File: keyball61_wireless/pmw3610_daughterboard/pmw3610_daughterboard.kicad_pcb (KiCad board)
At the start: 2 copper layers, 24 x 32 mm, 14 parts, among them J1 Conn_Keyball_8pin, U1 PMW3610DM-SUDU, U2 TLV74318PDBVR

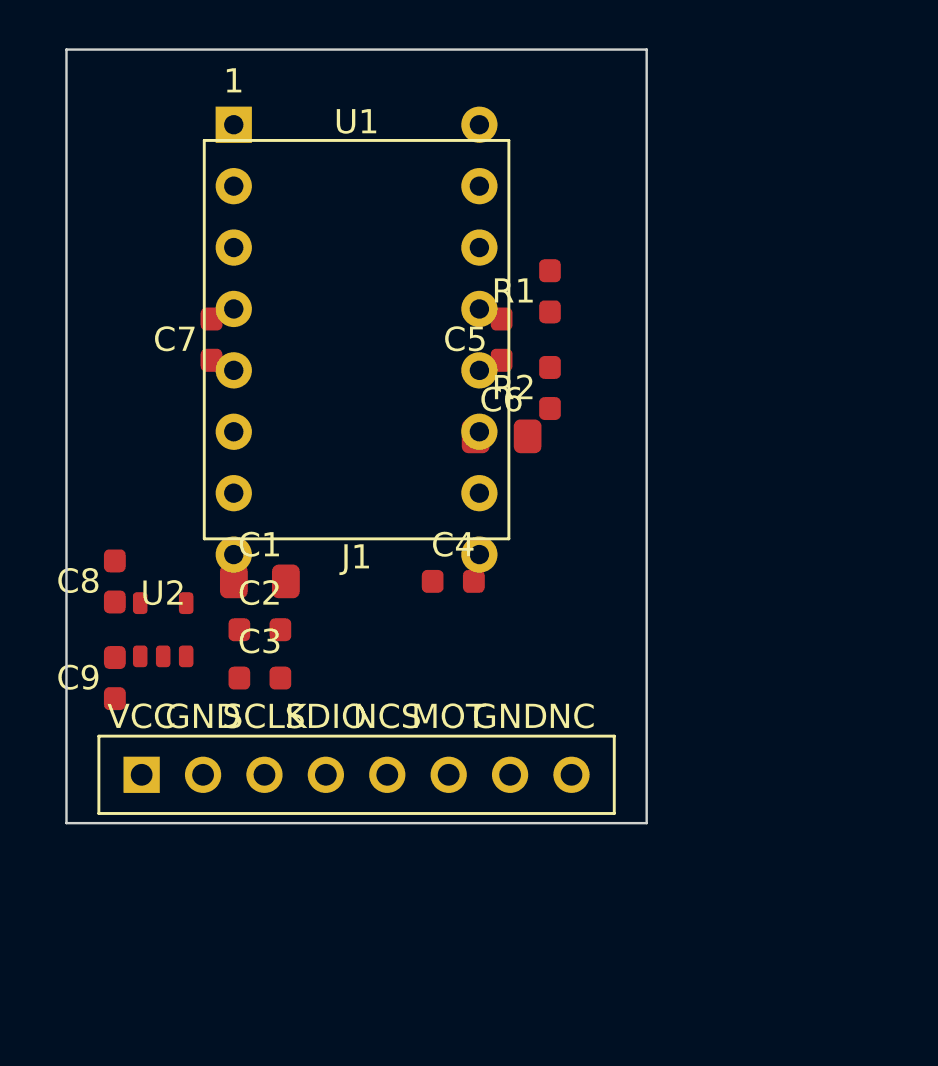
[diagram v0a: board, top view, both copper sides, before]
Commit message: Route PMW3610 daughterboard to DRC-clean fab-ready gerbers
Rebuilt the board with KiCad's native pcbnew API (replacing the kiutils
writer, which emitted KiCad-6 track syntax KiCad 10 rejected), auto-routed
with Freerouting 2.4.1 headless, imported the session, and exported gerbers.

Result: 0 DRC violations, 0 unconnected items. 14 components, 2-layer,
34x40mm, GND pour on B.Cu. Fab package zipped for PCBway.

Pipeline (reproducible):
- build_board.py  : place + net + design rules (pcbnew)
- export_dsn.py   : ExportSpecctraDSN
- Freerouting     : headless auto-route (.dsn -> .ses)
- import_ses.py   : ImportSpecctraSES + zone fill
- fix_track_width.py : widen any sub-0.25mm trace
- make_fab.sh     : end-to-end orchestration
- kicad-cli       : DRC + gerber/drill export

Outputs: gerbers/ (7 gerber + 4 drill), pmw3610_daughterboard_gerbers.zip,
board_top.png render.
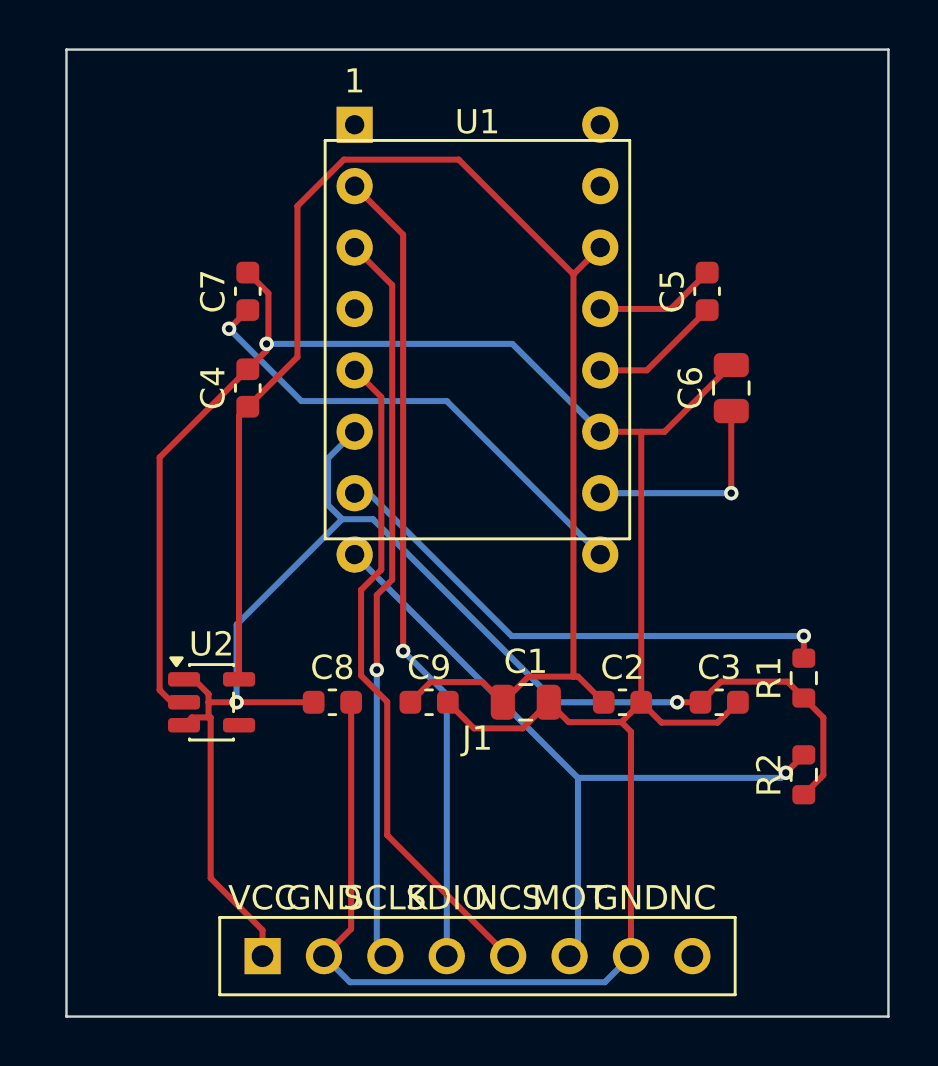
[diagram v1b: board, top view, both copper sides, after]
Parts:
- C1, C6: footprint Capacitor_SMD:C_0805_2012Metric -> C_0805_2012Metric
- C2, C3, C4, C5, C7, C8, C9: footprint Capacitor_SMD:C_0603_1608Metric -> C_0603_1608Metric
- J1: footprint pmw3610_kb:Conn_Keyball_8pin -> Conn_Keyball_8pin
- R1, R2: footprint Resistor_SMD:R_0603_1608Metric -> R_0603_1608Metric
- U1: footprint pmw3610_kb:PMW3610DM-SUDU -> PMW3610DM-SUDU
- U2: footprint Package_TO_SOT_SMD:SOT-23-5 -> SOT-23-5
- moved R1 19.1 mm to (30.5, 26.0)
- moved R2 19.1 mm to (30.5, 30.0)
- moved C3 19.0 mm to (27.0, 27.0)
- moved C2 15.3 mm to (23.0, 27.0)
- moved C9 13.0 mm to (15.0, 27.0), turned to 0 degrees
- moved C1 12.1 mm to (19.0, 27.0)
- moved C4 11.7 mm to (7.50, 14.0), turned to 90 degrees
- moved C8 10.3 mm to (11.0, 27.0), turned to 0 degrees
- moved C6 9.71 mm to (27.5, 14.0), turned to 90 degrees
- moved J1 9.01 mm to (17.0, 37.5)
- moved C5 8.73 mm to (26.5, 10.0)
- moved U1 5.00 mm to (17.0, 12.0)
- moved U2 3.61 mm to (6.00, 27.0)
- moved C7 2.50 mm to (7.50, 10.0)
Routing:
- net GND: track 0.00 -> 102.4 mm, vias 0 -> 1
- net +1V8: track 0.00 -> 62.5 mm
- net +3V3: track 0.00 -> 59.8 mm, vias 0 -> 2
- net SDIO: track 0.00 -> 33.4 mm, vias 0 -> 1
- net SCLK: track 0.00 -> 30.4 mm, vias 0 -> 1
- net MOTION: track 0.00 -> 30.3 mm, vias 0 -> 1
- net NCS: track 0.00 -> 27.6 mm
- net NRESET: track 0.00 -> 21.9 mm, vias 0 -> 1
- net VCP: track 0.00 -> 20.3 mm, vias 0 -> 1
- net PASST: track 0.00 -> 8.82 mm, vias 0 -> 1
- net CP: track 0.00 -> 5.45 mm
- net CN: track 0.00 -> 5.04 mm
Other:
- board size 24 x 32 mm -> 34 x 40 mm
- rule pad_to_mask_clearance: 0.0 -> 0

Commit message: Finalize PMW3610 daughterboard: datasheet-faithful, DRC-clean
23x25mm (orig 22x25 +1mm for on-pitch MOTION hole), 1.0mm, 2-layer.
- Lens slot sized to LM18-LSI (open to top edge) + guide-post hole
- Stock 7-pin connector at exact original positions + separate MOTION
  solder hole on the 2.54mm pitch, matched 1.5/0.9mm diameter
- Full PMW3610 circuit (TLV74318 LDO + charge-pump/decoupling caps),
  all parts above the connector (clears the 90-deg main-board joint)
- GND plane on B.Cu; rule-based placement (IPC-7351 spacing)
- 0 unrouted, 0 unconnected, 0 electrical DRC violations
  (4 courtyard-overlap advisories, not fab-blocking)

Reproducible pcbnew+Freerouting pipeline; gerbers zipped for PCBway.
Datasheets saved under pmw3610_datasheets/.
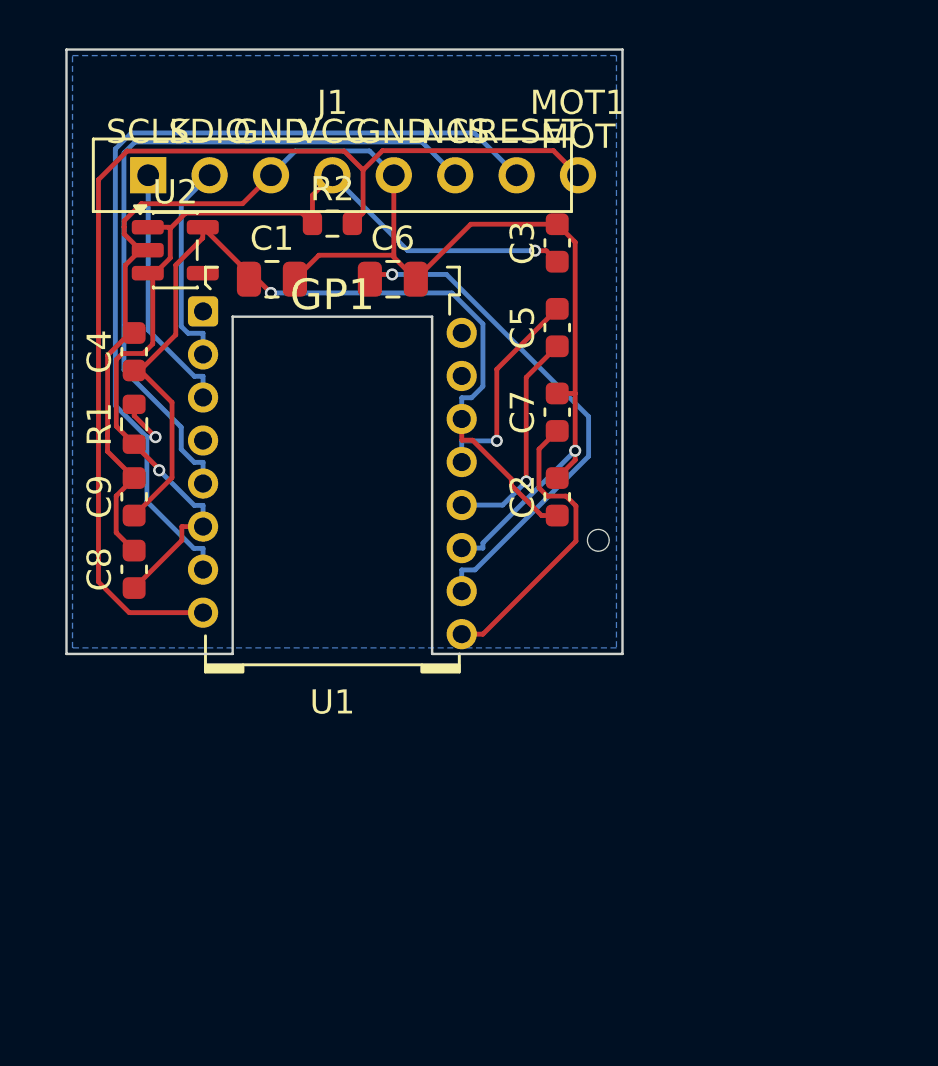
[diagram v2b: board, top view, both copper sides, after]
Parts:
- added GP1: , , F.Cu at (11.0, 10.2)
- added MOT1: MOTION, MOTION_solder_pad, F.Cu at (21.2, 5.20)
- J1: value Conn_Keyball_8pin -> Conn_Keyball_7pin; footprint Conn_Keyball_8pin -> Conn_Keyball_7pin_stock
- U1: footprint PMW3610DM-SUDU -> PMW3610DM-SUDU-siderakb
- moved J1 32.9 mm to (11.0, 5.20)
- moved R2 30.0 mm to (11.0, 7.20), turned to 0 degrees
- moved R1 29.6 mm to (2.80, 15.5)
- moved C1 20.4 mm to (8.50, 9.50)
- moved C3 20.1 mm to (20.3, 8.00), turned to 90 degrees
- moved U2 18.8 mm to (4.50, 8.30)
- moved C9 14.9 mm to (2.80, 18.5), turned to 90 degrees
- moved C6 14.7 mm to (13.5, 9.50), turned to 0 degrees
- moved C7 13.7 mm to (20.3, 15.0)
- moved C8 9.87 mm to (2.80, 21.5), turned to 90 degrees
- moved C2 8.92 mm to (20.3, 18.5), turned to 90 degrees
- moved U1 7.81 mm to (11.0, 17.0), turned to 90 degrees
- moved C5 6.38 mm to (20.3, 11.5)
- moved C4 4.93 mm to (2.80, 12.5)
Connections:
- C3 pad 1: +3V3 -> VCC
- C8 pad 1: +3V3 -> VCC
- J1 pad 1: +3V3 -> SCLK
- J1 pad 2: GND -> SDIO
- J1 pad 3: SCLK -> GND
- J1 pad 4: SDIO -> VCC
- J1 pad 5: NCS -> GND
- J1 pad 6: MOTION -> NCS
- J1 pad 7: GND -> NRESET
- R1 pad 1: +3V3 -> VCC
- R2 pad 1: +3V3 -> VCC
- U1 pad 6: +3V3 -> VCC
- U2 pad 1: +3V3 -> VCC
- U2 pad 3: +3V3 -> VCC
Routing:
- net +3V3: track 59.8 -> 0.00 mm, vias 2 -> 0
- net VCC: track 0.00 -> 40.4 mm, vias 0 -> 2
- net GND: track 102.4 -> 63.3 mm, vias 1 -> 4
- net SDIO: track 33.4 -> 8.64 mm, vias 1 -> 0
- net +1V8: track 62.5 -> 38.6 mm, vias 0 -> 1
- net SCLK: track 30.4 -> 10.3 mm, vias 1 -> 0
- net NRESET: track 21.9 -> 38.8 mm
- net MOTION: track 30.3 -> 45.3 mm, vias 1 -> 0
- net PASST: track 8.82 -> 21.3 mm
- net VCP: track 20.3 -> 12.3 mm, vias 1 -> 0
- net CN: track 5.04 -> 8.82 mm, vias 0 -> 1
- net CP: track 5.45 -> 9.20 mm, vias 0 -> 1
- net NCS: track 27.6 -> 29.7 mm
- added copper zone on B.Cu, net GND
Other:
- board size 34 x 40 mm -> 23 x 25 mm

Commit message: Relocate C1/C6 bulk caps clear of the optic/sensor pins
Moved the two 0805 bulk caps + MOTION pull-up out of the tight
sensor-adjacent area into the connector-to-sensor band: ~2mm clearance
from the sensor pins, well below the lens slot (no Z conflict with the
LM18-LSI optic). 0 electrical DRC violations; regenerated gerbers.
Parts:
- moved R2 5.01 mm to (16.0, 7.50)
- moved C1 2.06 mm to (9.00, 7.50)
- moved C6 2.06 mm to (13.0, 7.50)
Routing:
- net VCC: track 40.4 -> 63.4 mm, vias 2 -> 0
- net GND: track 63.3 -> 71.8 mm, vias 4 -> 6
- net SDIO: track 8.64 -> 15.1 mm, vias 0 -> 1
- net NRESET: track 38.8 -> 33.7 mm
- net MOTION: track 45.3 -> 42.1 mm
- net NCS: track 29.7 -> 32.1 mm
- net SCLK: track 10.3 -> 12.2 mm
- net PASST: track 21.3 -> 23.0 mm
- net +1V8: track 38.6 -> 40.2 mm, vias 1 -> 2
- net CP: track 9.20 -> 8.46 mm
- net CN: track 8.82 -> 8.22 mm

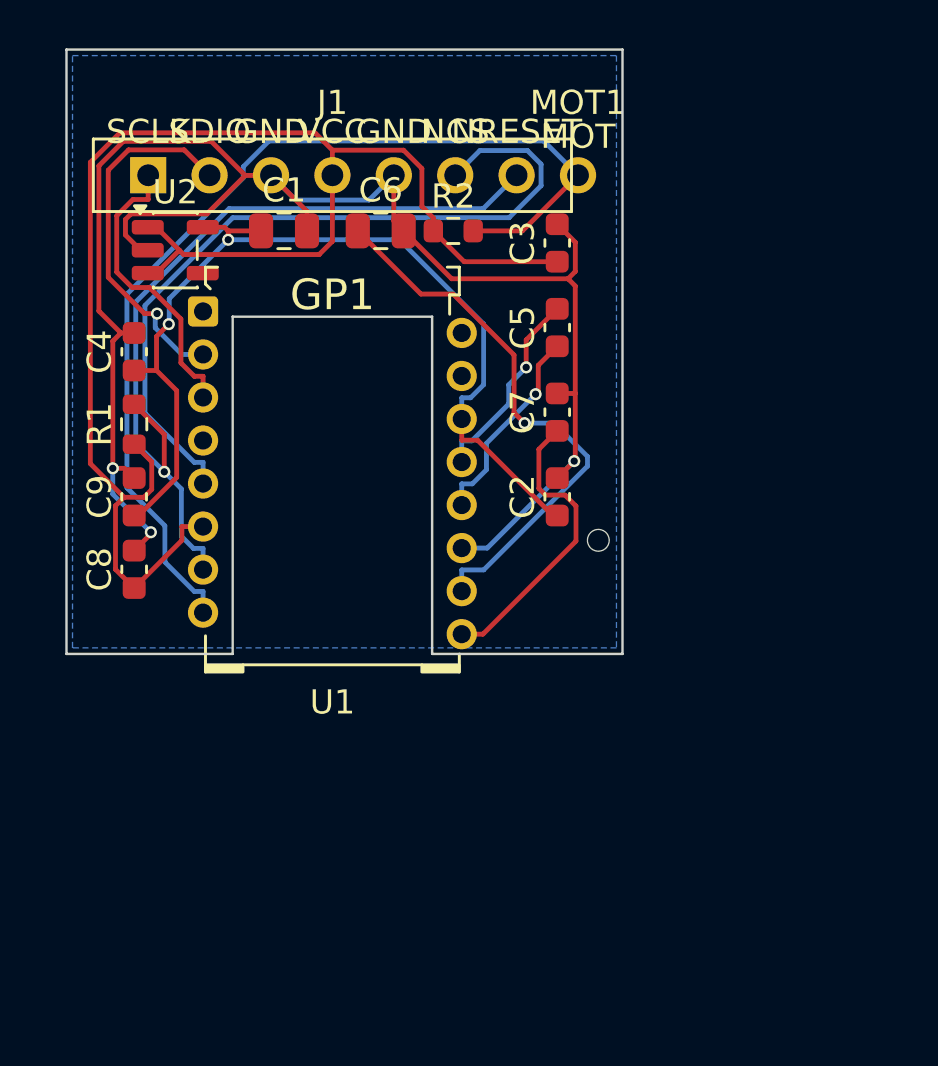
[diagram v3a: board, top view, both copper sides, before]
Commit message: Remove speculative PCB guide-post hole; regenerate fab package
The GP1 NPTH guide-post hole was both mislocated (a pcbnew pad/footprint
offset stacked it to the board corner) and unnecessary: per the PMW3610
datasheet Fig 5 and the LM18-LSI datasheet, the lens guide posts lock into
the SENSOR PACKAGE, not the PCB. Both siderakb and badjeff reference boards
have zero lens-alignment holes. Removing it clears the hole-clearance DRC
errors it caused.

Board now DRC-clean: 0 unconnected, 0 electrical, 0 hole-clearance (only
non-fatal courtyard-overlap advisories remain). Regenerated gerbers with a
clean fab layer set and separate PTH/NPTH Excellon drill files.
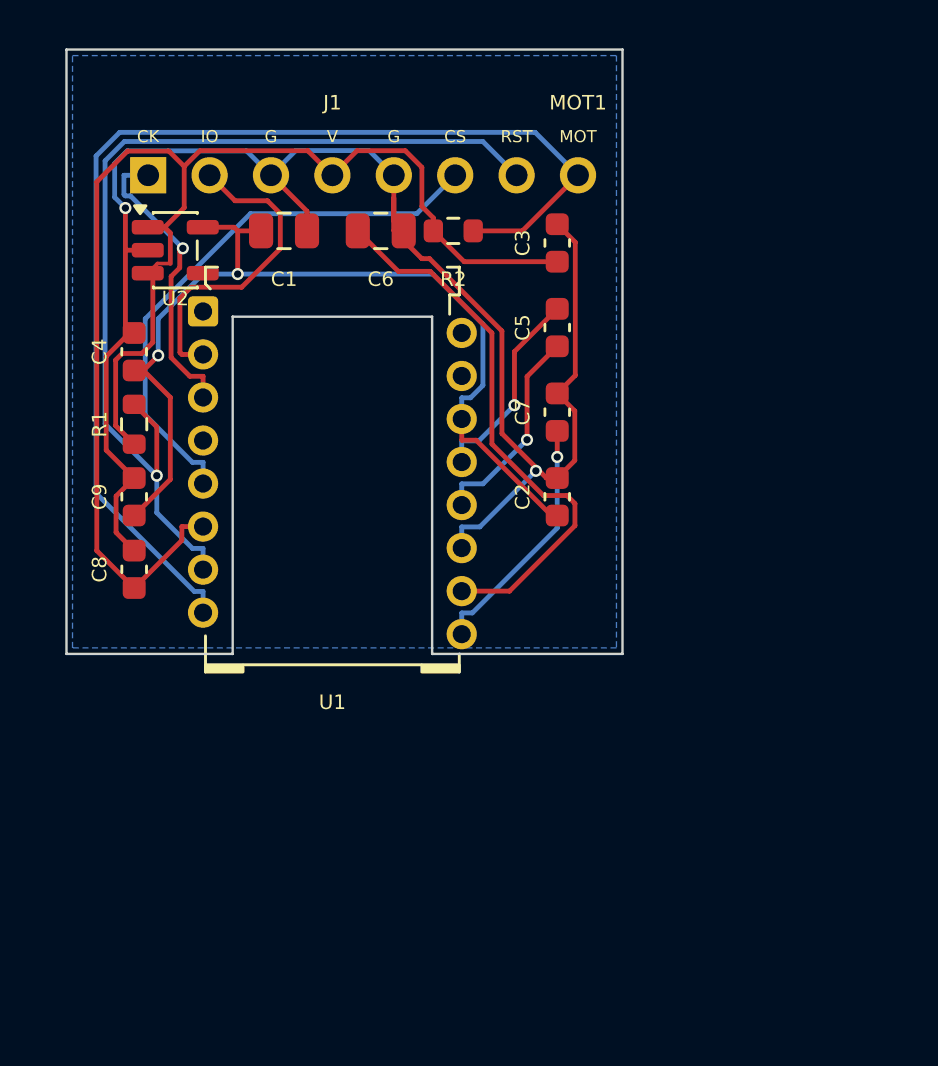
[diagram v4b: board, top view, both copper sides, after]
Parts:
- removed GP1: , 
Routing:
- net NCS: track 32.1 -> 23.3 mm
- net NRESET: track 33.7 -> 40.1 mm
- net MOTION: track 42.1 -> 47.3 mm
- net GND: track 71.8 -> 68.9 mm, vias 6 -> 5
- net VCC: track 63.4 -> 60.6 mm
- net VCP: track 12.3 -> 10.3 mm, vias 0 -> 1
- net SDIO: track 15.1 -> 13.3 mm, vias 1 -> 0
- net SCLK: track 12.2 -> 12.4 mm, vias 0 -> 1
- net PASST: track 23.0 -> 23.1 mm, vias 1 -> 0
